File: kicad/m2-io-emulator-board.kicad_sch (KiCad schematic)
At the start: 121 parts, among them J1 N2550-6002-RB, J10 61300811121, J11 61301011121, J12 Pin Header 02x18 2.54mm Verti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, J13 VGA femelle, J14 VIDEO, J2 N2526-6002-RB, J3 B10P-SHF-1AA, J4 B12P-SHF-1AA, J5 B12P-SHF-1AA, J6 61300811121, J7 61300811121, J8 61300811121, J9 61300811121, SW1 TEST, SW2 SERVICE, U1 ULN2803A, U2 74HCT86, U3 OPA3355EA

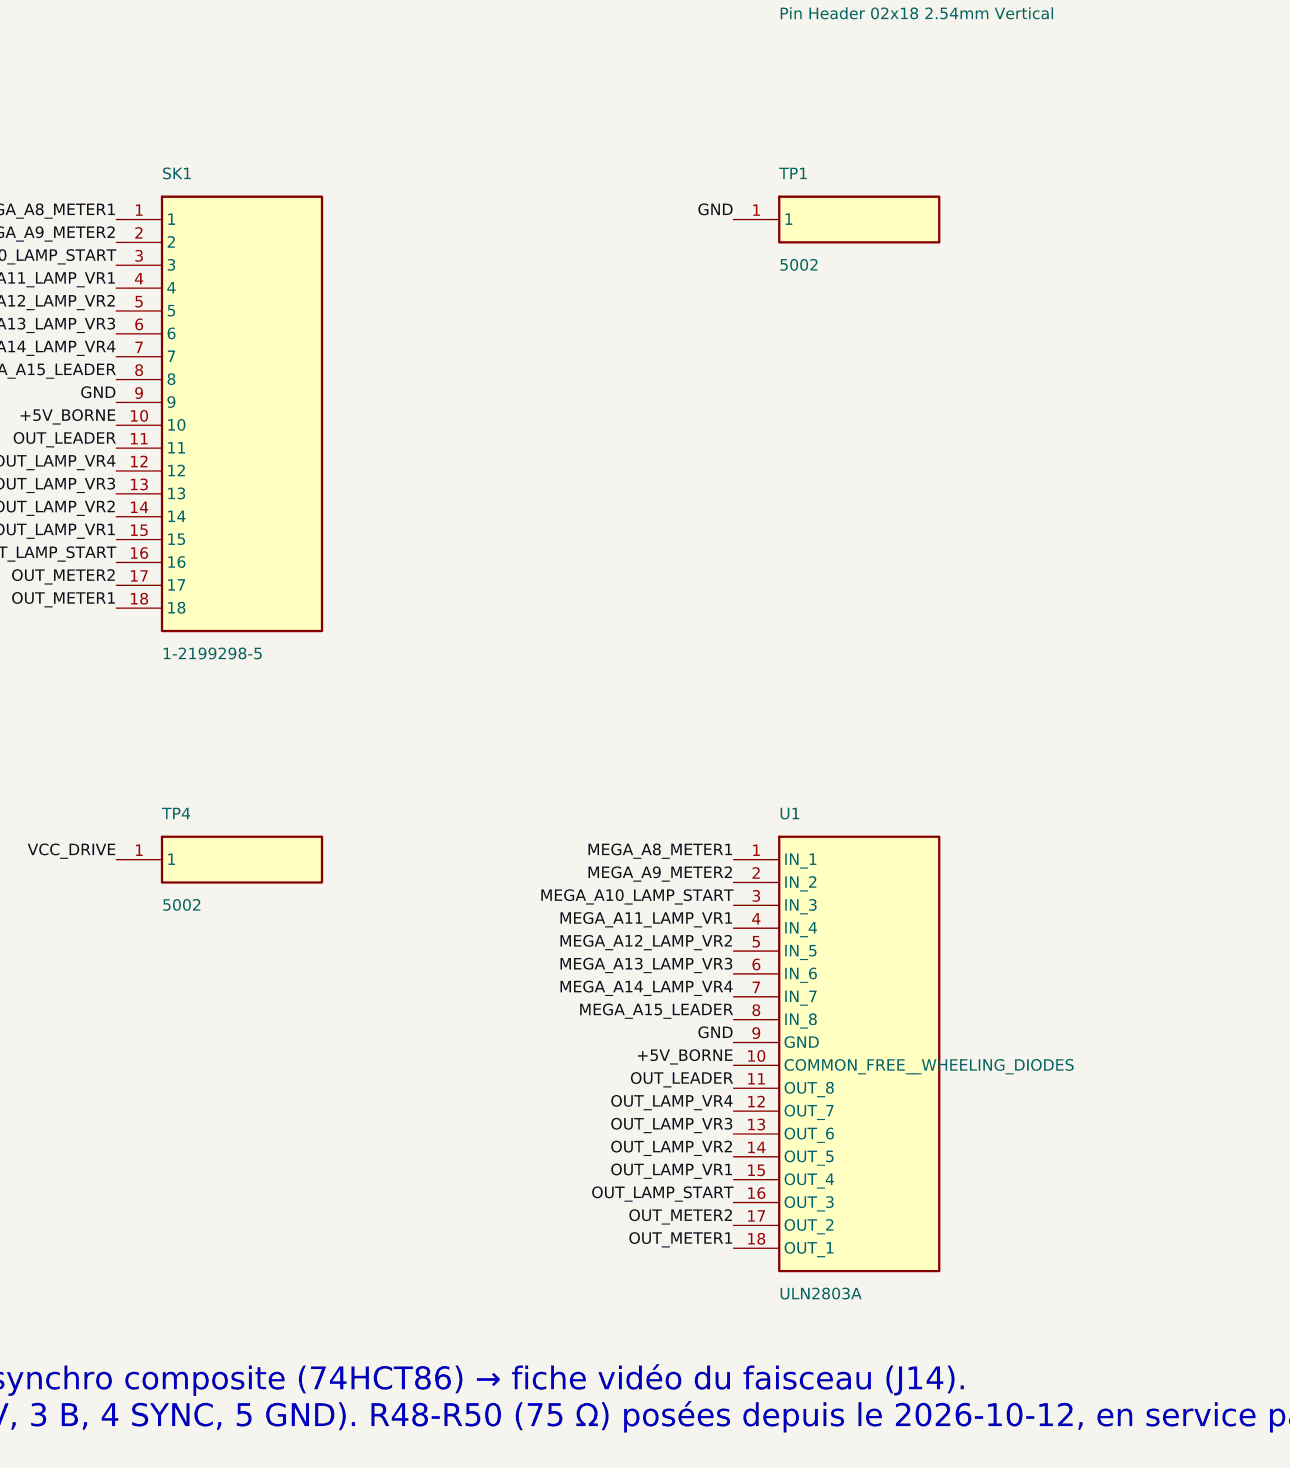
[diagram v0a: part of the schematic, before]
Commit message: U1 (ULN2803A) soldered directly: DIP-18 socket SK1 removed from schematic, PCB and BOM; Gerbers (silkscreen only), schematic PDF and renders updated
Co-Authored-By: Claude Opus 5.5 <noreply@anthropic.com>
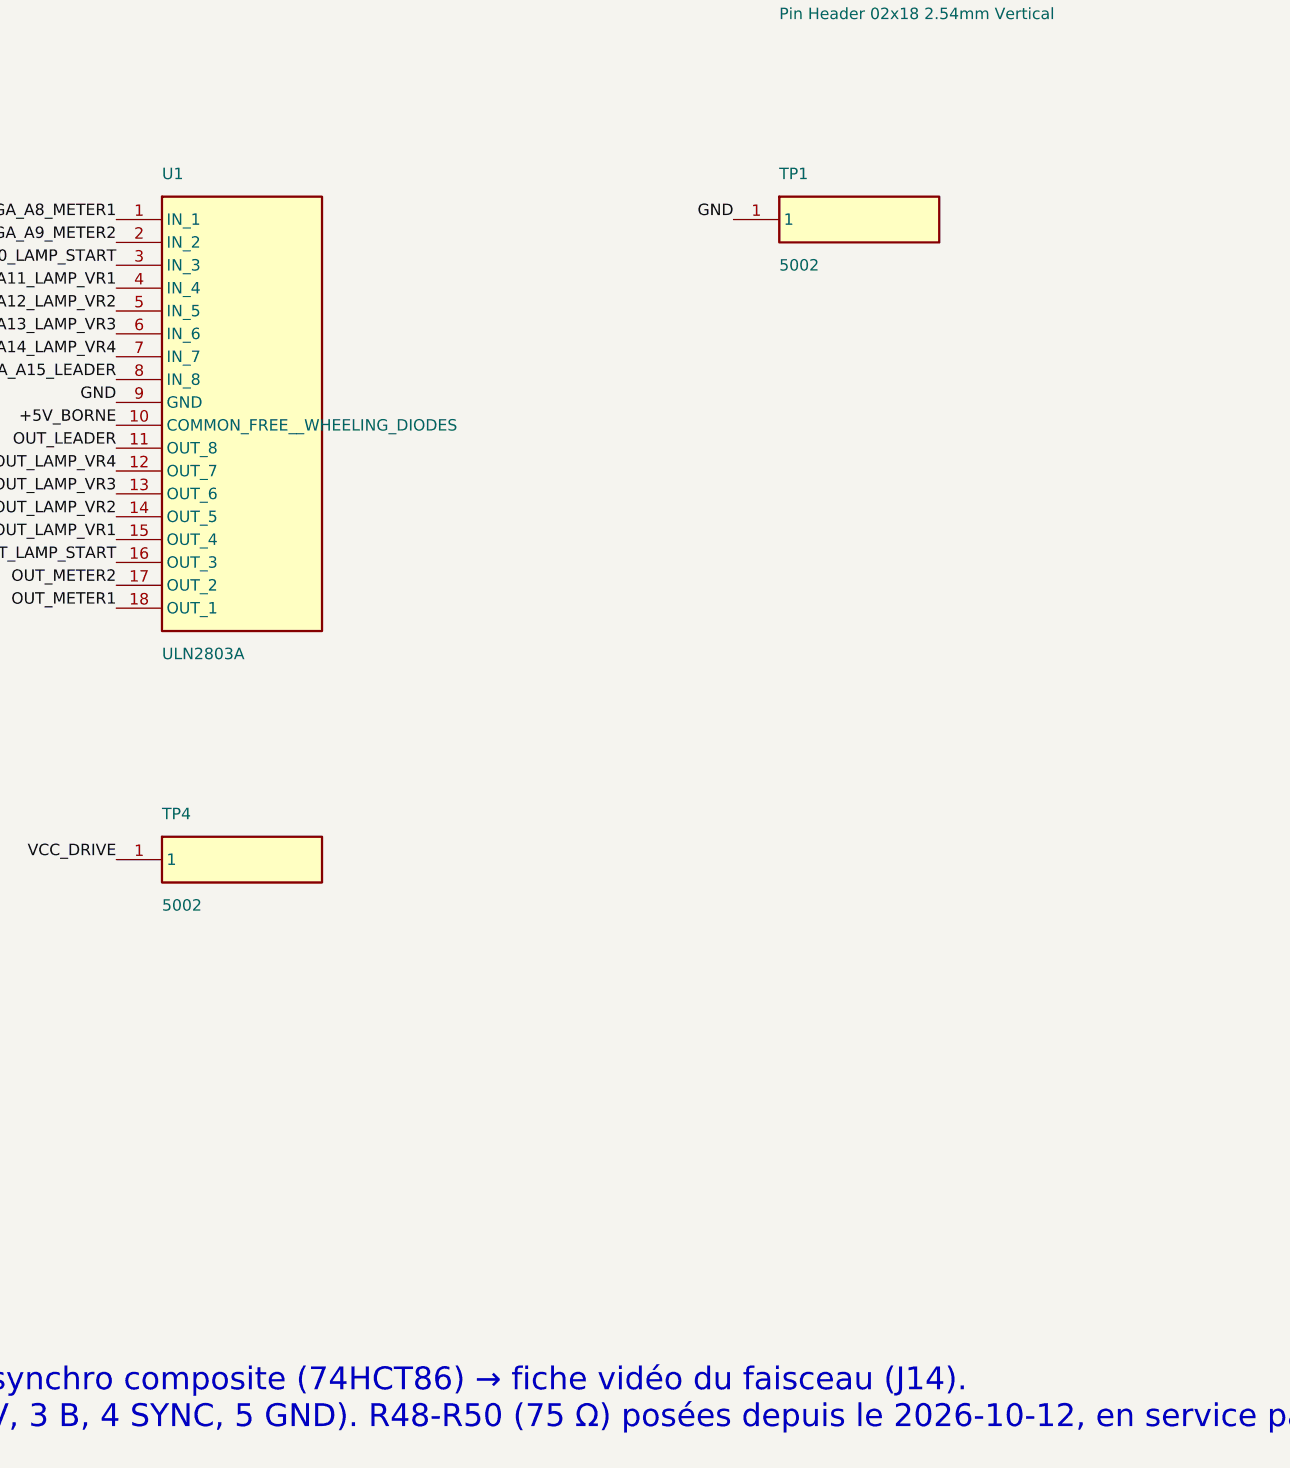
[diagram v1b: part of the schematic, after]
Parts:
- removed SK1: 1-2199298-5, Package_DIP:DIP-18_W7.62mm_Socket, symbol EDIF_SPC15500
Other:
- moved on the sheet: U1

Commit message: V2: screen jumper JP8 (Mega D36 to ground: ON = CRT 4:3, OFF = LVDS 16:9), framed silkscreen; Gerbers, drill files, schematic PDF, renders and BOM (EN/FR) updated
V1, the board ordered from JLCPCB on 2026-10-13, is tagged v1. JLCPCB BOM and CPL are unchanged (JP8 is through-hole).

Co-Authored-By: Claude Opus 5.5 <noreply@anthropic.com>
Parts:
- added JP8: 61300211121, Connector_PinHeader_2.54mm:PinHeader_1x02_P2.54mm_Vertical, symbol VIDEO_HDR_1x2
- added SH8: 382811-8, symbol EDIF__382811_8
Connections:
- net GND: now also JP8.2 (Pin_2)
- net MEGA_D36_ECRAN: now reaches J12.18 (Pin_17)
- net MEGA_D36_ECRAN: now also JP8.1 (Pin_1)
- no-connect marks 105 -> 106
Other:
- note added: "Choix de l'écran de l'hôte (2026-10-13, carte V2) : JP8 relie D36 du Mega (bit 1 de IN1, rappel interne) à la masse. Cavalier posé = HDMI vers le tube (24 kHz, 4:3) ; retiré = LVDS (16:9). Lu par l'hôte au démarrage, par le Mega."
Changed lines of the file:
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@@
 		(at 45.72 535.94)
 	)
-	(no_connect
-		(at 226.06 279.4)
-	)
+	(label "MEGA_D36_ECRAN" (at 226.06 279.40 180) (effects (font (size 1.27 1.27)) (justify right bottom)))
 	(no_connect
 		(at 88.9 63.5)
@@
 (label "+5V_MEGA" (at 162.56 745.49 90) (effects (font (size 1.27 1.27)) (justify left bottom)))
 (label "GND" (at 162.56 753.11 270) (effects (font (size 1.27 1.27)) (justify right bottom)))
+	(text "Choix de l'écran de l'hôte (2026-10-13, carte V2) : JP8 relie D36 du Mega (bit 1 de IN1, rappel interne) à la masse.\nCavalier posé = HDMI vers le tube (24 kHz, 4:3) ; retiré = LVDS (16:9). Lu par l'hôte au démarrage, par le Mega." (exclude_from_sim no) (at 25.40 769.62 0) (effects (font (size 2.54 2.54)) (justify left bottom)))
+(symbol (lib_id "VIDEO_HDR_1x2") (at 50.80 787.40 0) (unit 1) (body_style 1) (exclude_from_sim no) (in_bom yes) (on_board yes) (dnp no)
+(property "Reference" "JP8" (at 50.80 784.86 0) (effects (font (size 1.27 1.27)) (justify left)))
+(property "Value" "61300211121" (at 50.80 797.56 0) (effects (font (size 1.27 1.27)) (justify left)))
+(property "Footprint" "Connector_PinHeader_2.54mm:PinHeader_1x02_P2.54mm_Vertical" (at 50.80 787.40 0) (effects (font (size 1.27 1.27))) (hide yes))
+(property "Datasheet" "" (at 50.80 787.40 0) (effects (font (size 1.27 1.27))) (hide yes))
+(property "MPN" "61300211121" (at 50.80 787.40 0) (effects (font (size 1.27 1.27))) (hide yes))
+(property "Description" "Écran de l'hôte : cavalier posé = HDMI vers le tube (24 kHz, 4:3) ; retiré = LVDS (16:9). D36 du Mega, IN1 bit 1" (at 50.80 787.40 0) (effects (font (size 1.27 1.27))) (hide yes))
+(pin "1")(pin "2")
+(instances (project "m2-io-emulator-board" (path "/d44661bf-d01e-4075-8845-9c2310b0d4a5" (reference "JP8") (unit 1)))))
+(label "MEGA_D36_ECRAN" (at 45.72 789.94 180) (effects (font (size 1.27 1.27)) (justify right bottom)))
+(label "GND" (at 45.72 792.48 180) (effects (font (size 1.27 1.27)) (justify right bottom)))
+(symbol (lib_id "EDIF__382811_8") (at 91.44 787.40 0) (unit 1) (body_style 1) (exclude_from_sim no) (in_bom yes) (on_board no) (dnp no)
+(property "Reference" "SH8" (at 91.44 784.86 0) (effects (font (size 1.27 1.27)) (justify left)))
+(property "Value" "382811-8" (at 91.44 797.56 0) (effects (font (size 1.27 1.27)) (justify left)))
+(property "Footprint" "" (at 91.44 787.40 0) (effects (font (size 1.27 1.27))) (hide yes))
+(property "Datasheet" "" (at 91.44 787.40 0) (effects (font (size 1.27 1.27))) (hide yes))
+(property "MPN" "382811-8" (at 91.44 787.40 0) (effects (font (size 1.27 1.27))) (hide yes))
+(property "Description" "Cavalier de JP8" (at 91.44 787.40 0) (effects (font (size 1.27 1.27))) (hide yes))
+(pin "1")(pin "2")
+(instances (project "m2-io-emulator-board" (path "/d44661bf-d01e-4075-8845-9c2310b0d4a5" (reference "SH8") (unit 1)))))
+(no_connect (at 86.36 789.94))
+(no_connect (at 86.36 792.48))
 	(sheet_instances
 		(path "/"

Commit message: V3: HDMI input with on-board HDMI to VGA converter (CS5213), source jumper JP9, converter power jumper JP10, stereo RCA output, optional EDID EEPROM (DNP); Gerbers, drill files, schematic PDF, renders, BOM (EN/FR) and JLCPCB files updated
Co-Authored-By: Claude Opus 5.5 <noreply@anthropic.com>
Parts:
- added C24, C27, C28, C29, C31, C33, C35, C36, C38, C43, C44, C46: 100 nF, Capacitor_SMD:C_0805_2012Metric, symbol Device:C
- added C25, C26, C30, C32, C34, C37, C41, C42, C45: 10 µF, Capacitor_SMD:C_0805_2012Metric, symbol Device:C
- added C39, C40: 10 nF, Capacitor_SMD:C_0805_2012Metric, symbol Device:C
- added FB1: 600 Ω @ 100 MHz, Inductor_SMD:L_0805_2012Metric, symbol VIDEO_FERRITE
- added J15: HDMI A, Connector_Video:HDMI_A_Amphenol_10029449-x01xLF_Horizontal, symbol VIDEO_HDMI_A
- added J16: RCJ-2223, interface-borne:CUI_RCJ-22xx_RCA_Dual_Horizontal, symbol VIDEO_RCA_DUAL
- added JP10: 61300311121, Connector_PinHeader_2.54mm:PinHeader_1x03_P2.54mm_Vertical, symbol EDIF__61300311121
- added JP9: 61300211121, Connector_PinHeader_2.54mm:PinHeader_1x02_P2.54mm_Vertical, symbol VIDEO_HDR_1x2
- added R60: 1 kΩ, Resistor_SMD:R_0805_2012Metric, symbol Device:R
- added R61, R62, R63, R64, R65: 10 kΩ, Resistor_SMD:R_0805_2012Metric, symbol Device:R
- added SH10, SH9: 382811-8, symbol EDIF__382811_8
- added U4: CS5213, Package_DFN_QFN:QFN-32-1EP_4x4mm_P0.4mm_EP2.65x2.65mm, symbol VIDEO_CS5213
- added U5: NX3303X, Package_DFN_QFN:QFN-32-1EP_5x5mm_P0.5mm_EP3.1x3.1mm, symbol VIDEO_NX3303X
- added U6: AT24C02, Package_SO:SOIC-8_3.9x4.9mm_P1.27mm, symbol VIDEO_24C02
- added U7: TS5V330, Package_SO:TSSOP-16_4.4x5mm_P0.65mm, symbol VIDEO_TS5V330
- added U8: 74HCT157, Package_SO:SOIC-16_3.9x9.9mm_P1.27mm, symbol VIDEO_74HCT157
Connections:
- net +5V_BORNE: now also FB1.1
- net +5V_MEGA: now also C43.1, C44.1, JP10.1 (Pin_1), R61.2, U7.16 (VCC), U8.16 (VCC)
- net GND: now also C24.2, C25.2, C26.2, C27.2, C28.2, C29.2, C30.2, C31.2, C32.2, C33.2, C34.2, C35.2, C36.2, C37.2, C38.2, C39.2, C40.2, C43.2, C44.2, C45.2, C46.2, J15.11 (CKS), J15.17 (GND), J15.2 (D2S), J15.5 (D1S), J15.8 (D0S), J15.SH (SHIELD), J16.1 (BARREL), JP9.2 (Pin_2), R62.2, R63.2, R64.2, R65.2, U4.33 (EPAD), U5.23 (GND), U5.33 (EPAD), U6.1 (A0), U6.2 (A1), U6.3 (A2), U6.4 (GND), U6.7 (WP), U7.12 (DD), U7.13 (S2D), U7.14 (S1D), U7.15 (~EN), U7.8 (GND), U8.10 (3B), U8.11 (3A), U8.13 (4B), U8.14 (4A), U8.15 (~G), U8.8 (GND)
- net VGA_B: now also U7.9 (DC); no longer J13.3 (B)
- net VGA_G: now also U7.7 (DB); no longer J13.2 (V)
- net VGA_HS: now also U8.4 (1Y); no longer J13.13 (HSYNC)
- net VGA_R: now also U7.4 (DA); no longer J13.1 (R)
- net VGA_VS: now also U8.7 (2Y); no longer J13.14 (VSYNC)
- new net +5V_BORNE_F: C45.1, C46.1, FB1.2, JP10.3 (Pin_3)
- new net +5V_CONV: C25.1, C32.1, C33.1, JP10.2 (Pin_2), U4.10 (VDD5_IN), U5.22 (VDD5)
- new net AUD_OUT_L: C41.2, J16.2 (X2_BAS)
- new net AUD_OUT_R: C42.2, J16.3 (X1_HAUT)
- new net CS_3V3: C26.1, C27.1, C28.1, C29.1, U4.15 (VDD33), U4.16 (AUDIO_EN), U4.20 (VDD33_VDAC), U4.21 (AVD_ADAC), U4.32 (VDD33), U4.9 (VDD33_OUT)
- new net CS_AUD_VREF: C30.1, C31.1, U4.23 (AUD_VREF)
- new net HDMI_5V: C24.1, J15.18 (+5V), R60.2, U6.8 (VCC)
- new net HDMI_CK_N: J15.12 (CK-), U4.1 (HDMI_CKN), U5.1 (RX_CK-)
- new net HDMI_CK_P: J15.10 (CK+), U4.2 (HDMI_CKP), U5.2 (RX_CK+)
- new net HDMI_D0_N: J15.9 (D0-), U4.3 (HDMI_D0N), U5.4 (RX_D0-)
- new net HDMI_D0_P: J15.7 (D0+), U4.4 (HDMI_D0P), U5.5 (RX_D0+)
- new net HDMI_D1_N: J15.6 (D1-), U4.5 (HDMI_D1N), U5.7 (RX_D1-)
- new net HDMI_D1_P: J15.4 (D1+), U4.6 (HDMI_D1P), U5.8 (RX_D1+)
- new net HDMI_D2_N: J15.3 (D2-), U4.7 (HDMI_D2N), U5.9 (RX_D2-)
- new net HDMI_D2_P: J15.1 (D2+), U4.8 (HDMI_D2P), U5.10 (RX_D2+)
- new net HDMI_HPD: J15.19 (HPD), R60.1
- new net HDMI_SCL: J15.15 (SCL), U6.6 (SCL)
- new net HDMI_SDA: J15.16 (SDA), U6.5 (SDA)
- new net HD_AUD_L: C39.1, C41.1, U4.24 (AUD_L), U5.17 (AOUTL)
- new net HD_AUD_R: C40.1, C42.1, U4.22 (AUD_R), U5.18 (AOUTR)
- new net HD_B: U4.17 (VGA_B), U5.12 (B), U7.11 (S1C)
- new net HD_G: U4.18 (VGA_G), U5.13 (G), U7.5 (S1B)
- new net HD_HS: R62.1, U4.12 (VGA_HS), U5.27 (HSYNC), U8.2 (1A)
- new net HD_R: U4.19 (VGA_R), U5.14 (R), U7.2 (S1A)
- new net HD_VS: R63.1, U4.11 (VGA_VS), U5.24 (VSYNC), U8.5 (2A)
- new net J13_B: J13.3 (B), U7.10 (S2C)
- new net J13_G: J13.2 (V), U7.6 (S2B)
- new net J13_HS: J13.13 (HSYNC), R64.1, U8.3 (1B)
- new net J13_R: J13.1 (R), U7.3 (S2A)
- new net J13_VS: J13.14 (VSYNC), R65.1, U8.6 (2B)
- new net NX_1V2: C37.1, C38.1, U5.20 (LDO1V2), U5.3 (VDD12), U5.31 (DVDD12)
- new net NX_3V3: C34.1, C35.1, C36.1, U5.11 (VDD33), U5.15 (VDD33), U5.19 (VDD33), U5.21 (LDO3V3), U5.32 (VDD33), U5.6 (VDD33)
- new net SRC_SEL: JP9.1 (Pin_1), R61.1, U7.1 (IN), U8.1 (~A/B)
- no-connect marks 106 -> 129
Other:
- note added: "V3 (2026-10-15, non publiée) : HDMI → VGA intégré. J15 HDMI → U4 CS5213 OU U5 NX3303X (jamais les deux) → U7/U8. JP9 SOURCE : posé = HDMI, retiré = VGA J13 (comme la V2). Sorties = VGA_R/G/B/HS/VS (U2, U3, JP2-JP4 inchangés). JP10 alim de la puce : 1-2 = +5V_MEGA, 2-3 = +5V_BORNE filtré (FB1). U6 EEPROM d'EDID prévue, non posée. Audio de la puce → J16 double RCA (haut rouge = D, bas blanc = G)."
